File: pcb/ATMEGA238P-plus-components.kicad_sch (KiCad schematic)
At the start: 70 parts, among them J15 ICSP, J16 USB_B_Micro, J17 Conn_Coaxial, SW3 TC-6610_C7528713, U3 ATMEGA328P-AU, U4 CH340G, U5 LM358DR, U6 74HC245, U7 nRF24L01P, U8 MICROSD_C164170, U9 74AHC1G125, Y3 16MHz, Y4 12MHz, Y5 16MHz

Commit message: pcb: SW1-SW3 go SMD - TS-1088 (C720477, Basic) supersedes the 6x6 THT tacts
Smaller-footprint request: ~5.6x3.0 mm single-side land vs a 6x6 body with
four through-holes, freeing bottom copper under all three buttons on the
2-layer board. Basic library kills one Extended feeder line and three
hand-solder THT parts. Pad map CLEAN (2 pads <-> 2 pins, no shorted-pair
topology). Board sync via F8 + replace-footprints to follow.
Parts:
- SW3: value TC-6610_C7528713 -> TS-1088-AR02016_C720477; footprint Button_Switch_THT:SW_PUSH_6mm_H9.5mm -> easyeda:SW-SMD_L3.9-W3.0-P4.45; LCSC C7528713 -> C720477; Manufacturer FG -> XUNPU; Part TC-6610 -6*6*9-260g -> TS-1088-AR02016
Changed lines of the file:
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@@
 			)
 		)
-		(property "Value" "TC-6610_C7528713"
+		(property "Value" "TS-1088-AR02016_C720477"
 			(at 33.02 40.6399 90)
 			(hide yes)
@@
 			)
 		)
-		(property "Footprint" "Button_Switch_THT:SW_PUSH_6mm_H9.5mm"
+		(property "Footprint" "easyeda:SW-SMD_L3.9-W3.0-P4.45"
 			(at 34.29 39.37 0)
 			(hide yes)
@@
 			)
 		)
-		(property "Datasheet" "https://wmsc.lcsc.com/wmsc/upload/file/pdf/v2/lcsc/2401191746_FG-TC-6610--6-6-9-260g_C7528713.pdf"
+		(property "Datasheet" "https://www.lcsc.com/datasheet/lcsc_datasheet_2304140030_XUNPU-TS-1088-AR02016_C720477.pdf"
 			(at 34.29 39.37 0)
 			(hide yes)
@@
 			)
 		)
-		(property "LCSC" "C7528713"
+		(property "LCSC" "C720477"
 			(at 29.21 39.37 0)
 			(hide yes)
@@
 			)
 		)
-		(property "Part" "TC-6610 -6*6*9-260g"
+		(property "Part" "TS-1088-AR02016"
 			(at 29.21 39.37 0)
 			(hide yes)
@@
 			)
 		)
-		(property "Manufacturer" "FG"
+		(property "Manufacturer" "XUNPU"
 			(at 29.21 39.37 0)
 			(hide yes)

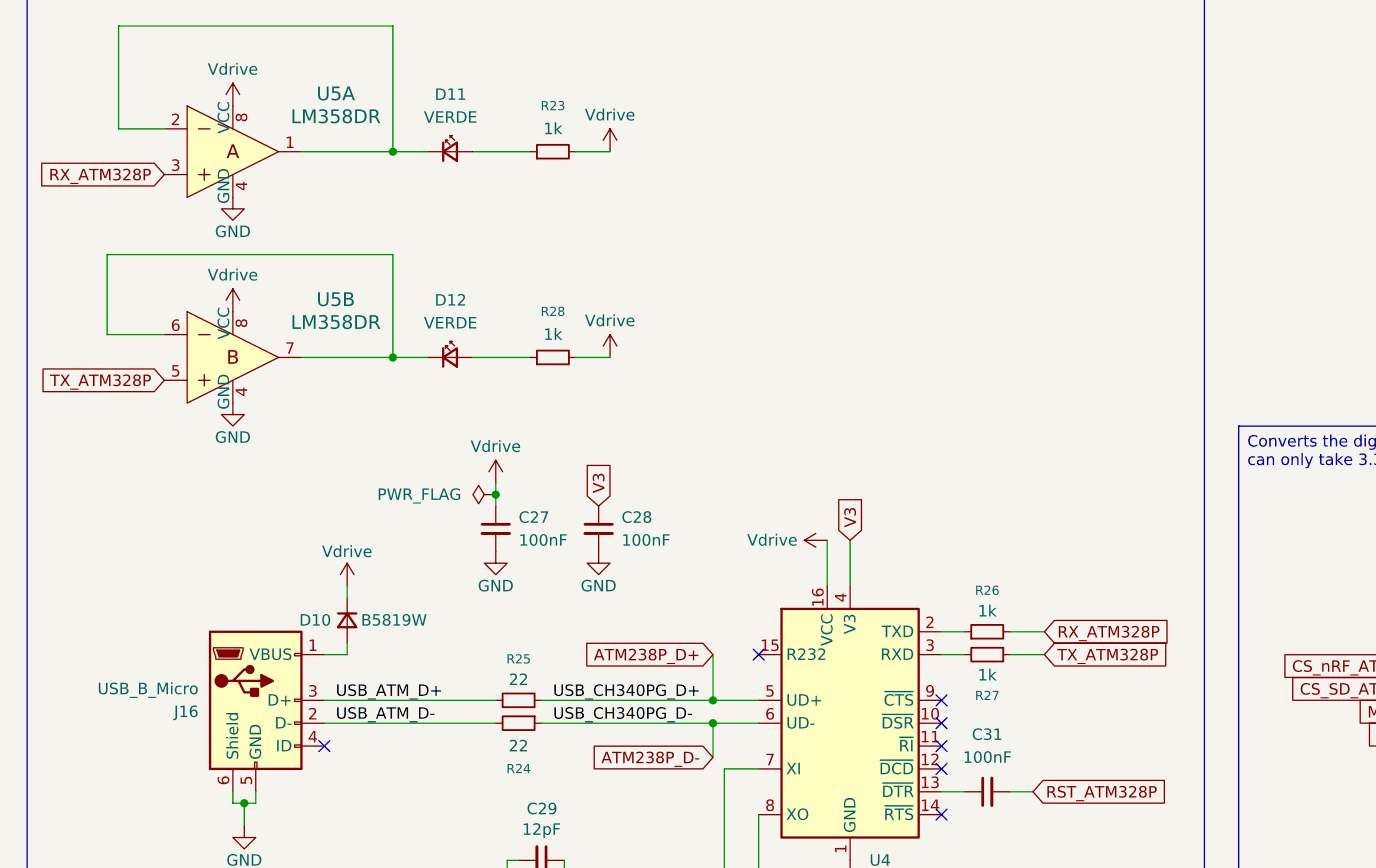
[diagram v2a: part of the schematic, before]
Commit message: finish drone controller pcb first pass
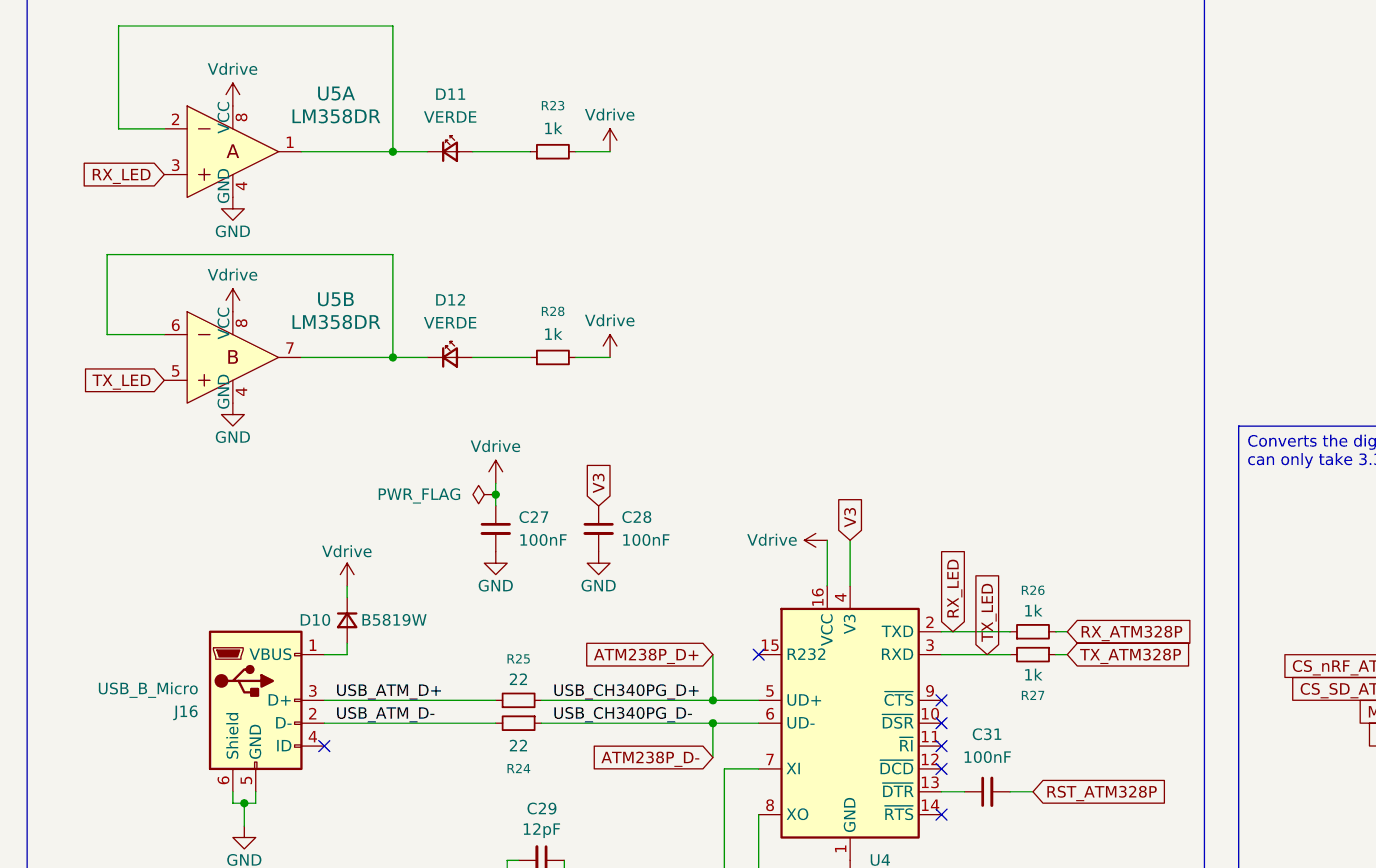
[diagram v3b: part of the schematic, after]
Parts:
- R24, R25: footprint Resistor_SMD:R_0402_1005Metric -> Resistor_SMD:R_0603_1608Metric
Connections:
- net RX_ATM328P: no longer U5.3
- net TX_ATM328P: no longer U5.5
- net RX_LED: now reaches R26.1, U4.2 (TXD)
- net RX_LED: now also U5.3
- net TX_LED: now reaches R27.2, U4.3 (RXD)
- net TX_LED: now also U5.5
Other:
- moved on the sheet: R26, R27
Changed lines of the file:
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@@
 	(wire
 		(pts
-			(xy 127 241.3) (xy 123.19 241.3)
+			(xy 129.54 241.3) (xy 128.27 241.3)
 		)
 		(stroke
@@
 	(wire
 		(pts
-			(xy 127 238.76) (xy 123.19 238.76)
+			(xy 129.54 238.76) (xy 128.27 238.76)
 		)
 		(stroke
@@
 	(wire
 		(pts
-			(xy 118.11 238.76) (xy 115.57 238.76)
+			(xy 123.19 238.76) (xy 115.57 238.76)
 		)
 		(stroke
@@
 	(wire
 		(pts
-			(xy 118.11 241.3) (xy 115.57 241.3)
-		)
-		(stroke
-			(width 0)
-			(type default)
-		)
-	)
-	(wire
-		(pts
 			(xy 149.86 22.86) (xy 161.29 22.86)
 		)
@@
 	(wire
 		(pts
+			(xy 115.57 241.3) (xy 123.19 241.3)
+		)
+		(stroke
+			(width 0)
+			(type default)
+		)
+	)
+	(wire
+		(pts
 			(xy 67.31 264.16) (xy 67.31 269.24)
 		)
@@
 		)
 	)
+	(global_label "TX_LED"
+		(shape input)
+		(at 120.65 241.3 90)
+		(fields_autoplaced yes)
+		(effects
+			(font
+				(size 1.27 1.27)
+			)
+			(justify left)
+		)
+		(property "Intersheetrefs" "${INTERSHEET_REFS}"
+			(at 120.65 231.723 90)
+			(hide yes)
+			(show_name no)
+			(do_not_autoplace no)
+			(effects
+				(font
+					(size 1.27 1.27)
+				)
+				(justify left)
+			)
+		)
+	)
 	(global_label "NRF_ANT1"
 		(shape input)
@@
 	(global_label "RX_ATM328P"
 		(shape input)
-		(at 127 238.76 0)
+		(at 129.54 238.76 0)
 		(fields_autoplaced yes)
 		(effects
@@
 		)
 		(property "Intersheetrefs" "${INTERSHEET_REFS}"
-			(at 141.8384 238.76 0)
+			(at 144.3784 238.76 0)
 			(hide yes)
 			(show_name no)
@@
 		)
 	)
+	(global_label "RX_LED"
+		(shape input)
+		(at 116.84 238.76 90)
+		(fields_autoplaced yes)
+		(effects
+			(font
+				(size 1.27 1.27)
+			)
+			(justify left)
+		)
+		(property "Intersheetrefs" "${INTERSHEET_REFS}"
+			(at 116.84 228.8806 90)
+			(hide yes)
+			(show_name no)
+			(do_not_autoplace no)
+			(effects
+				(font
+					(size 1.27 1.27)
+				)
+				(justify left)
+			)
+		)
+	)
 	(global_label "CS_SD_74HC245"
 		(shape input)
@@
 		)
 	)
-	(global_label "TX_ATM328P"
+	(global_label "TX_LED"
 		(shape input)
 		(at 29.21 210.82 180)
@@
 		)
 		(property "Intersheetrefs" "${INTERSHEET_REFS}"
-			(at 14.674 210.82 0)
+			(at 19.633 210.82 0)
 			(hide yes)
 			(show_name no)
@@
 		)
 	)
-	(global_label "RX_ATM328P"
+	(global_label "RX_LED"
 		(shape input)
 		(at 29.21 187.96 180)
@@
 		)
 		(property "Intersheetrefs" "${INTERSHEET_REFS}"
-			(at 14.3716 187.96 0)
+			(at 19.3306 187.96 0)
 			(hide yes)
 			(show_name no)
@@
 	(global_label "TX_ATM328P"
 		(shape input)
-		(at 127 241.3 0)
+		(at 129.54 241.3 0)
 		(fields_autoplaced yes)
 		(effects
@@
 		)
 		(property "Intersheetrefs" "${INTERSHEET_REFS}"
-			(at 141.536 241.3 0)
+			(at 144.076 241.3 0)
 			(hide yes)
 			(show_name no)
@@
 	(symbol
 		(lib_id "Device:R_Small")
-		(at 120.65 238.76 90)
+		(at 125.73 238.76 90)
 		(unit 1)
 		(body_style 1)
@@
 		(dnp no)
 		(property "Reference" "R26"
-			(at 120.65 234.188 90)
+			(at 125.73 234.188 90)
 			(show_name no)
 			(do_not_autoplace no)
@@
 		)
 		(property "Value" "1k"
-			(at 120.65 236.474 90)
+			(at 125.73 236.474 90)
 			(show_name no)
 			(do_not_autoplace no)
@@
 		)
 		(property "Footprint" "Resistor_SMD:R_0402_1005Metric"
-			(at 120.65 238.76 0)
+			(at 125.73 238.76 0)
 			(hide yes)
 			(show_name no)
@@
 		)
 		(property "Datasheet" "https://www.lcsc.com/datasheet/lcsc_datasheet_2206010216_UNI-ROYAL-Uniroyal-Elec-0402WGF1001TCE_C11702.pdf"
-			(at 120.65 238.76 0)
+			(at 125.73 238.76 0)
 			(hide yes)
 			(show_name no)
@@
 		)
 		(property "Description" "Resistor, small symbol"
-			(at 120.65 238.76 0)
+			(at 125.73 238.76 0)
 			(hide yes)
 			(show_name no)
@@
 		)
 		(property "LCSC" "C11702"
-			(at 120.65 238.76 0)
+			(at 125.73 238.76 0)
 			(hide yes)
 			(show_name no)
@@
 		)
 		(property "Part" "0402WGF1001TCE"
-			(at 120.65 238.76 0)
+			(at 125.73 238.76 0)
 			(hide yes)
 			(show_name no)
@@
 		)
 		(property "Manufacturer" "UNI-ROYAL(Uniroyal Elec)"
-			(at 120.65 238.76 0)
+			(at 125.73 238.76 0)
 			(hide yes)
 			(show_name no)
@@
 			)
 		)
-		(property "Footprint" "Resistor_SMD:R_0402_1005Metric"
+		(property "Footprint" "Resistor_SMD:R_0603_1608Metric"
 			(at 68.58 246.38 0)
 			(hide yes)
@@
 			)
 		)
-		(property "Footprint" "Resistor_SMD:R_0402_1005Metric"
+		(property "Footprint" "Resistor_SMD:R_0603_1608Metric"
 			(at 68.58 248.92 0)
 			(hide yes)
@@
 	(symbol
 		(lib_id "Device:R_Small")
-		(at 120.65 241.3 270)
+		(at 125.73 241.3 270)
 		(unit 1)
 		(body_style 1)
@@
 		(dnp no)
 		(property "Reference" "R27"
-			(at 120.65 245.872 90)
+			(at 125.73 245.872 90)
 			(show_name no)
 			(do_not_autoplace no)
@@
 		)
 		(property "Value" "1k"
-			(at 120.65 243.586 90)
+			(at 125.73 243.586 90)
 			(show_name no)
 			(do_not_autoplace no)
@@
 		)
 		(property "Footprint" "Resistor_SMD:R_0402_1005Metric"
-			(at 120.65 241.3 0)
+			(at 125.73 241.3 0)
 			(hide yes)
 			(show_name no)
@@
 		)
 		(property "Datasheet" "https://www.lcsc.com/datasheet/lcsc_datasheet_2206010216_UNI-ROYAL-Uniroyal-Elec-0402WGF1001TCE_C11702.pdf"
-			(at 120.65 241.3 0)
+			(at 125.73 241.3 0)
 			(hide yes)
 			(show_name no)
@@
 		)
 		(property "Description" "Resistor, small symbol"
-			(at 120.65 241.3 0)
+			(at 125.73 241.3 0)
 			(hide yes)
 			(show_name no)
@@
 		)
 		(property "LCSC" "C11702"
-			(at 120.65 241.3 0)
+			(at 125.73 241.3 0)
 			(hide yes)
 			(show_name no)
@@
 		)
 		(property "Part" "0402WGF1001TCE"
-			(at 120.65 241.3 0)
+			(at 125.73 241.3 0)
 			(hide yes)
 			(show_name no)
@@
 		)
 		(property "Manufacturer" "UNI-ROYAL(Uniroyal Elec)"
-			(at 120.65 241.3 0)
+			(at 125.73 241.3 0)
 			(hide yes)
 			(show_name no)
